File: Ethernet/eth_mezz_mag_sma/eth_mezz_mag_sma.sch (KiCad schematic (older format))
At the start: 13 parts, among them J1 Conn_01x09_Male, J2 TX-, J3 RX+, J4 RX-, J5 TX+

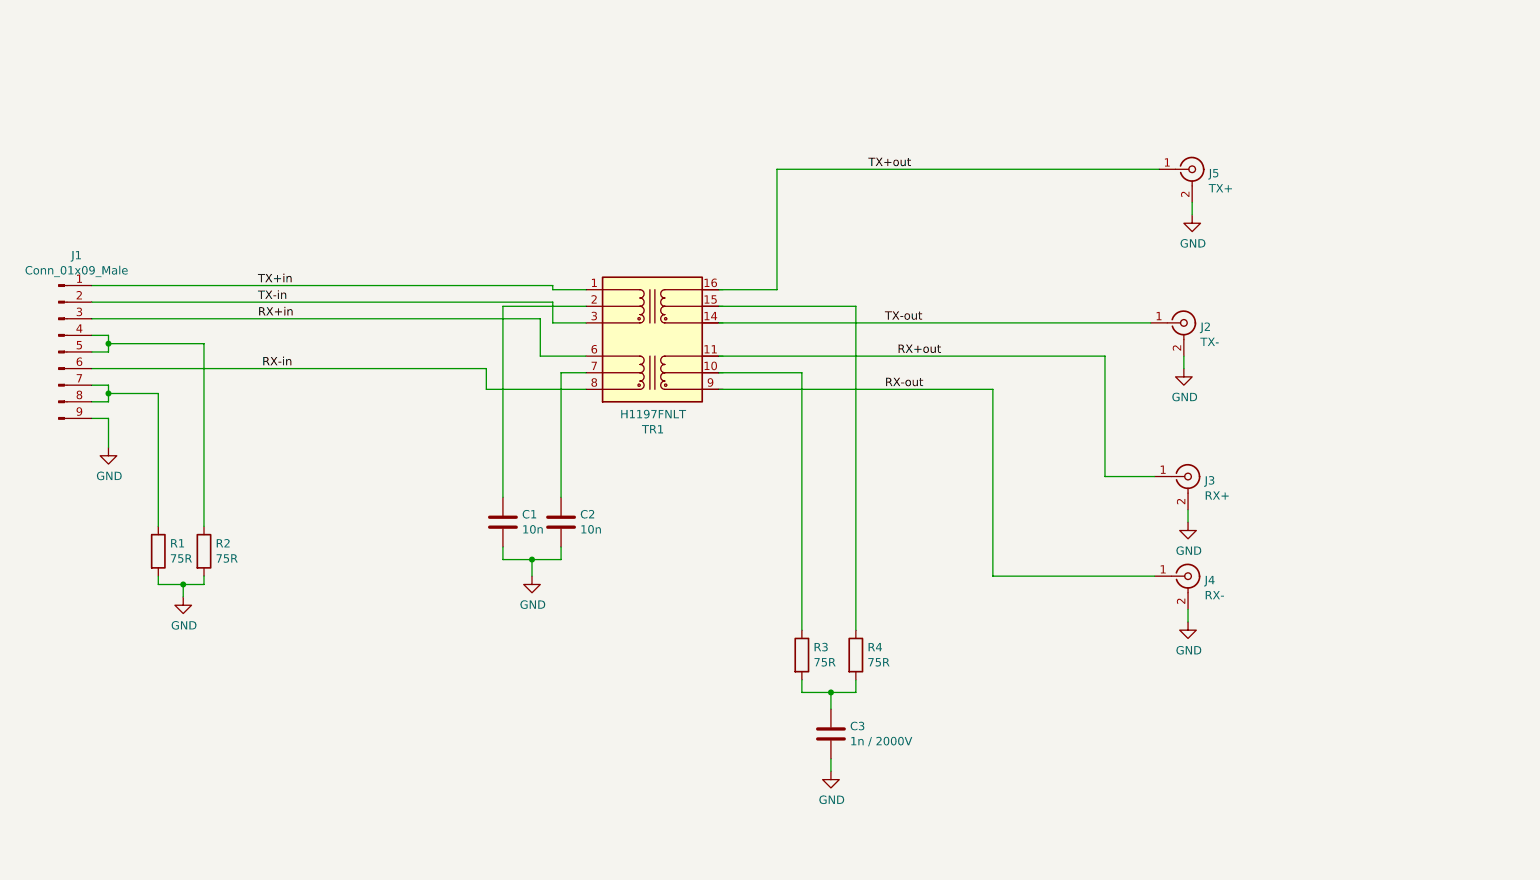
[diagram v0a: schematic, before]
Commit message: PHY module with RJ45
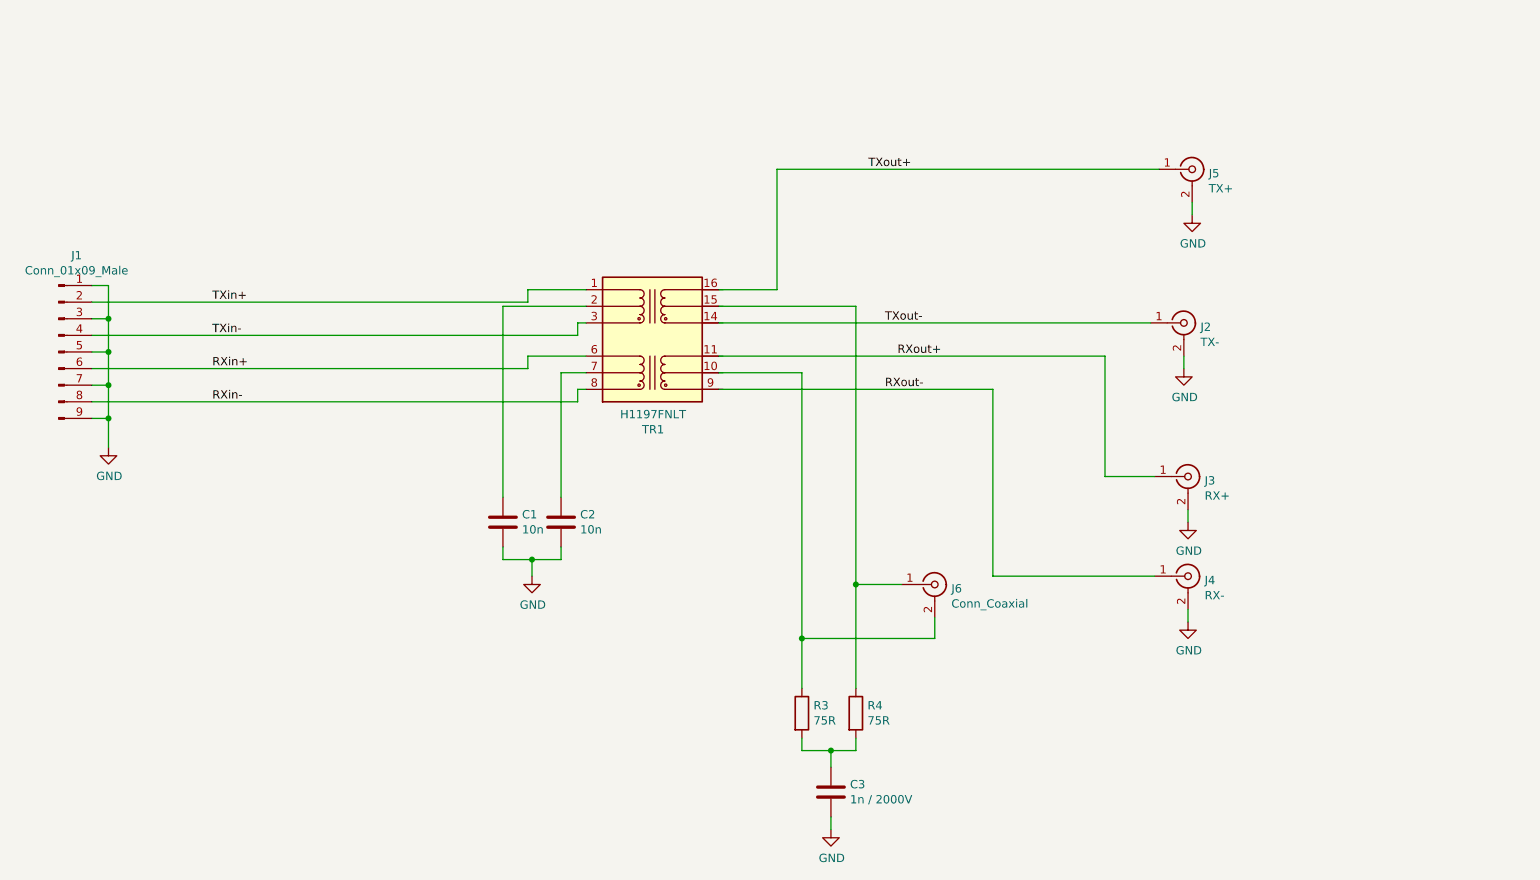
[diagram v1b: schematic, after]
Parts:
- removed R1, R2: 75R, Resistor_SMD:R_1206_3216Metric_Pad1.42x1.75mm_HandSolder, symbol Device:R
- added J6: Conn_Coaxial, Connector_Coaxial:BNC_TEConnectivity_1478204_Vertical, symbol Connector:Conn_Coaxial
- C1, C2: footprint Resistor_SMD:R_1206_3216Metric_Pad1.42x1.75mm_HandSolder -> Capacitor_SMD:C_0805_2012Metric_Pad1.18x1.45mm_HandSolder
- R3, R4: footprint Resistor_SMD:R_1206_3216Metric_Pad1.42x1.75mm_HandSolder -> Resistor_SMD:R_0805_2012Metric_Pad1.20x1.40mm_HandSolder
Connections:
- net GND: now also J1.1 (Pin_1), J1.3 (Pin_3), J1.5 (Pin_5), J1.7 (Pin_7)
- net at R3.1, TR1.10 (C_RX): now also J6.2 (Ext)
- net at R4.1, TR1.15 (C_TX): now also J6.1 (In)
- net TXin-: now reaches J1.4 (Pin_4)
- net TXin-: now also TR1.3 (TD-); no longer J1.5 (Pin_5)
- net RXin-: now reaches J1.8 (Pin_8)
- net RXin-: now also TR1.8 (RD-); no longer J1.7 (Pin_7)
- net RX+in renamed RXin+
- net RXin+: now also J1.6 (Pin_6); no longer J1.3 (Pin_3)
- net RX+out renamed RXout+
- removed net RX-in: J1.6 (Pin_6), TR1.8 (RD-)
- net RX-out renamed RXout-
- net TX+in renamed TXin+
- net TXin+: now also J1.2 (Pin_2); no longer J1.1 (Pin_1)
- net TX+out renamed TXout+
- removed net TX-in: J1.2 (Pin_2), TR1.3 (TD-)
- net TX-out renamed TXout-
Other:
- moved on the sheet: C3, R3, R4
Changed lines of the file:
@@
 L Device:R R3
 U 1 1 61BAD53E
-P 6275 4975
-F 0 "R3" H 6345 5021 50  0000 L CNN
-F 1 "75R" H 6345 4930 50  0000 L CNN
-F 2 "Resistor_SMD:R_1206_3216Metric_Pad1.42x1.75mm_HandSolder" V 6205 4975 50  0001 C CNN
-F 3 "~" H 6275 4975 50  0001 C CNN
-	1    6275 4975
+P 6275 5325
+F 0 "R3" H 6345 5371 50  0000 L CNN
+F 1 "75R" H 6345 5280 50  0000 L CNN
+F 2 "Resistor_SMD:R_0805_2012Metric_Pad1.20x1.40mm_HandSolder" V 6205 5325 50  0001 C CNN
+F 3 "~" H 6275 5325 50  0001 C CNN
+	1    6275 5325
 	1    0    0    -1
 $EndComp
@@
 L Device:R R4
 U 1 1 61BADB8B
-P 6600 4975
-F 0 "R4" H 6670 5021 50  0000 L CNN
-F 1 "75R" H 6670 4930 50  0000 L CNN
-F 2 "Resistor_SMD:R_1206_3216Metric_Pad1.42x1.75mm_HandSolder" V 6530 4975 50  0001 C CNN
-F 3 "~" H 6600 4975 50  0001 C CNN
-	1    6600 4975
+P 6600 5325
+F 0 "R4" H 6670 5371 50  0000 L CNN
+F 1 "75R" H 6670 5280 50  0000 L CNN
+F 2 "Resistor_SMD:R_0805_2012Metric_Pad1.20x1.40mm_HandSolder" V 6530 5325 50  0001 C CNN
+F 3 "~" H 6600 5325 50  0001 C CNN
+	1    6600 5325
 	1    0    0    -1
 $EndComp
@@
 L Device:C C3
 U 1 1 61BAE2C0
-P 6450 5450
-F 0 "C3" H 6565 5496 50  0000 L CNN
-F 1 "1n / 2000V" H 6565 5405 50  0000 L CNN
-F 2 "Resistor_SMD:R_1206_3216Metric_Pad1.42x1.75mm_HandSolder" H 6488 5300 50  0001 C CNN
-F 3 "~" H 6450 5450 50  0001 C CNN
-	1    6450 5450
+P 6450 5800
+F 0 "C3" H 6565 5846 50  0000 L CNN
+F 1 "1n / 2000V" H 6565 5755 50  0000 L CNN
+F 2 "Resistor_SMD:R_1206_3216Metric_Pad1.42x1.75mm_HandSolder" H 6488 5650 50  0001 C CNN
+F 3 "~" H 6450 5800 50  0001 C CNN
+	1    6450 5800
 	1    0    0    -1
 $EndComp
@@
 F 0 "C1" H 4590 4221 50  0000 L CNN
 F 1 "10n" H 4590 4130 50  0000 L CNN
-F 2 "Resistor_SMD:R_1206_3216Metric_Pad1.42x1.75mm_HandSolder" H 4513 4025 50  0001 C CNN
+F 2 "Capacitor_SMD:C_0805_2012Metric_Pad1.18x1.45mm_HandSolder" H 4513 4025 50  0001 C CNN
 F 3 "~" H 4475 4175 50  0001 C CNN
 	1    4475 4175
@@
 F 0 "C2" H 4940 4221 50  0000 L CNN
 F 1 "10n" H 4940 4130 50  0000 L CNN
-F 2 "Resistor_SMD:R_1206_3216Metric_Pad1.42x1.75mm_HandSolder" H 4863 4025 50  0001 C CNN
+F 2 "Capacitor_SMD:C_0805_2012Metric_Pad1.18x1.45mm_HandSolder" H 4863 4025 50  0001 C CNN
 F 3 "~" H 4825 4175 50  0001 C CNN
 	1    4825 4175
@@
 $EndComp
 Wire Wire Line
-	2000 2750 4775 2750
-Wire Wire Line
-	4775 2750 4775 2775
-Wire Wire Line
-	4775 2775 4975 2775
-Wire Wire Line
-	2000 2850 4775 2850
-Wire Wire Line
-	4775 2850 4775 2975
-Wire Wire Line
-	4775 2975 4975 2975
-Wire Wire Line
-	2000 2950 4700 2950
-Wire Wire Line
-	4700 2950 4700 3175
-Wire Wire Line
-	4700 3175 4975 3175
-Wire Wire Line
-	2000 3250 4375 3250
-Wire Wire Line
-	4375 3250 4375 3375
-Wire Wire Line
-	4375 3375 4975 3375
-Wire Wire Line
 	5775 2775 6125 2775
 Wire Wire Line
@@
 Wire Wire Line
 	7425 4500 8400 4500
-Wire Wire Line
-	4975 3275 4825 3275
-Wire Wire Line
-	4825 3275 4825 4025
-Wire Wire Line
-	4975 2875 4475 2875
-Wire Wire Line
-	4475 2875 4475 4025
-$Comp
-L Device:R R1
-U 1 1 61BB773B
-P 2400 4350
-F 0 "R1" H 2470 4396 50  0000 L CNN
-F 1 "75R" H 2470 4305 50  0000 L CNN
-F 2 "Resistor_SMD:R_1206_3216Metric_Pad1.42x1.75mm_HandSolder" V 2330 4350 50  0001 C CNN
-F 3 "~" H 2400 4350 50  0001 C CNN
-	1    2400 4350
-	1    0    0    -1
-$EndComp
-Wire Wire Line
-	2000 3050 2100 3050
-Wire Wire Line
-	2100 3050 2100 3100
-Wire Wire Line
-	2100 3150 2000 3150
-Wire Wire Line
-	2000 3350 2100 3350
-Wire Wire Line
-	2100 3350 2100 3400
-Wire Wire Line
-	2100 3450 2000 3450
 $Comp
 L power:GND #PWR01
@@
 Wire Wire Line
 	2000 3550 2100 3550
-Wire Wire Line
-	2100 3550 2100 3725
-Wire Wire Line
-	2400 4200 2400 3400
-Wire Wire Line
-	2400 3400 2100 3400
-Connection ~ 2100 3400
-Wire Wire Line
-	2100 3400 2100 3450
-$Comp
-L Device:R R2
-U 1 1 61BBA3B7
-P 2675 4350
-F 0 "R2" H 2745 4396 50  0000 L CNN
-F 1 "75R" H 2745 4305 50  0000 L CNN
-F 2 "Resistor_SMD:R_1206_3216Metric_Pad1.42x1.75mm_HandSolder" V 2605 4350 50  0001 C CNN
-F 3 "~" H 2675 4350 50  0001 C CNN
-	1    2675 4350
-	1    0    0    -1
-$EndComp
-Wire Wire Line
-	2675 4200 2675 3100
-Wire Wire Line
-	2675 3100 2100 3100
-Connection ~ 2100 3100
-Wire Wire Line
-	2100 3100 2100 3150
-$Comp
-L power:GND #PWR02
-U 1 1 61BBB0D3
-P 2550 4625
-F 0 "#PWR02" H 2550 4375 50  0001 C CNN
-F 1 "GND" H 2555 4452 50  0000 C CNN
-F 2 "" H 2550 4625 50  0001 C CNN
-F 3 "" H 2550 4625 50  0001 C CNN
-	1    2550 4625
-	1    0    0    -1
-$EndComp
-Wire Wire Line
-	2400 4500 2400 4550
-Wire Wire Line
-	2400 4550 2550 4550
-Wire Wire Line
-	2675 4550 2675 4500
-Connection ~ 2550 4550
-Wire Wire Line
-	2550 4550 2675 4550
-Wire Wire Line
-	2550 4550 2550 4625
 $Comp
 L power:GND #PWR03
@@
 	5775 2875 6600 2875
 Wire Wire Line
-	6600 2875 6600 4825
+	6600 2875 6600 4550
 Wire Wire Line
 	5775 3275 6275 3275
 Wire Wire Line
-	6275 3275 6275 4825
-Wire Wire Line
-	6275 5125 6275 5200
-Wire Wire Line
-	6275 5200 6450 5200
-Wire Wire Line
-	6600 5200 6600 5125
-Wire Wire Line
-	6450 5300 6450 5200
-Connection ~ 6450 5200
-Wire Wire Line
-	6450 5200 6600 5200
+	6275 3275 6275 4875
+Wire Wire Line
+	6275 5475 6275 5550
+Wire Wire Line
+	6275 5550 6450 5550
+Wire Wire Line
+	6600 5550 6600 5475
+Wire Wire Line
+	6450 5650 6450 5550
+Connection ~ 6450 5550
+Wire Wire Line
+	6450 5550 6600 5550
 $Comp
 L power:GND #PWR04
 U 1 1 61BC3E53
-P 6450 5675
-F 0 "#PWR04" H 6450 5425 50  0001 C CNN
-F 1 "GND" H 6455 5502 50  0000 C CNN
-F 2 "" H 6450 5675 50  0001 C CNN
-F 3 "" H 6450 5675 50  0001 C CNN
-	1    6450 5675
-	1    0    0    -1
-$EndComp
-Wire Wire Line
-	6450 5600 6450 5675
+P 6450 6025
+F 0 "#PWR04" H 6450 5775 50  0001 C CNN
+F 1 "GND" H 6455 5852 50  0000 C CNN
+F 2 "" H 6450 6025 50  0001 C CNN
+F 3 "" H 6450 6025 50  0001 C CNN
+	1    6450 6025
+	1    0    0    -1
+$EndComp
+Wire Wire Line
+	6450 5950 6450 6025
 $Comp
 L power:GND #PWR07
@@
 Wire Wire Line
 	8600 4700 8600 4775
-Text Label 3000 2750 0    50   ~ 0
-TX+in
-Text Label 3000 2850 0    50   ~ 0
-TX-in
-Text Label 3000 2950 0    50   ~ 0
-RX+in
-Text Label 3025 3250 0    50   ~ 0
-RX-in
+Text Label 2725 2850 0    50   ~ 0
+TXin+
+Text Label 2725 3050 0    50   ~ 0
+TXin-
+Text Label 2725 3250 0    50   ~ 0
+RXin+
+Text Label 2725 3450 0    50   ~ 0
+RXin-
 Text Label 6675 2050 0    50   ~ 0
-TX+out
+TXout+
 Text Label 6775 2975 0    50   ~ 0
-TX-out
+TXout-
 Text Label 6850 3175 0    50   ~ 0
-RX+out
+RXout+
 Text Label 6775 3375 0    50   ~ 0
-RX-out
+RXout-
+Wire Wire Line
+	2000 2850 4625 2850
+Wire Wire Line
+	4625 2850 4625 2775
+Wire Wire Line
+	4625 2775 4975 2775
+Wire Wire Line
+	2000 3050 4925 3050
+Wire Wire Line
+	4925 3050 4925 2975
+Wire Wire Line
+	4925 2975 4975 2975
+Wire Wire Line
+	2000 3250 4625 3250
+Wire Wire Line
+	4625 3250 4625 3175
+Wire Wire Line
+	4625 3175 4975 3175
+Wire Wire Line
+	2000 3450 4925 3450
+Wire Wire Line
+	4925 3450 4925 3375
+Wire Wire Line
+	4925 3375 4975 3375
+Wire Wire Line
+	4975 3275 4825 3275
+Wire Wire Line
+	4825 3275 4825 4025
+Wire Wire Line
+	4975 2875 4475 2875
+Wire Wire Line
+	4475 2875 4475 4025
+Wire Wire Line
+	2000 2750 2100 2750
+Wire Wire Line
+	2100 2750 2100 2950
+Connection ~ 2100 3550
+Wire Wire Line
+	2100 3550 2100 3725
+Wire Wire Line
+	2000 2950 2100 2950
+Connection ~ 2100 2950
+Wire Wire Line
+	2100 2950 2100 3150
+Wire Wire Line
+	2000 3150 2100 3150
+Connection ~ 2100 3150
+Wire Wire Line
+	2100 3150 2100 3350
+Wire Wire Line
+	2000 3350 2100 3350
+Connection ~ 2100 3350
+Wire Wire Line
+	2100 3350 2100 3550
+$Comp
+L Connector:Conn_Coaxial J6
+U 1 1 61BA50FC
+P 7075 4550
+F 0 "J6" H 7175 4525 50  0000 L CNN
+F 1 "Conn_Coaxial" H 7175 4434 50  0000 L CNN
+F 2 "Connector_Coaxial:BNC_TEConnectivity_1478204_Vertical" H 7075 4550 50  0001 C CNN
+F 3 " ~" H 7075 4550 50  0001 C CNN
+	1    7075 4550
+	1    0    0    -1
+$EndComp
+Wire Wire Line
+	6875 4550 6600 4550
+Connection ~ 6600 4550
+Wire Wire Line
+	6600 4550 6600 5175
+Wire Wire Line
+	7075 4750 7075 4875
+Wire Wire Line
+	7075 4875 6275 4875
+Connection ~ 6275 4875
+Wire Wire Line
+	6275 4875 6275 5175
 $EndSCHEMATC

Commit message: SomeBoardsReady
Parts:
- added H1, H2: MountingHole_Pad, MountingHole:MountingHole_3.2mm_M3_Pad_Via, symbol Mechanical:MountingHole_Pad
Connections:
- net labels added: RCT, TCT
- wire segments 60 -> 66
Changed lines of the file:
@@
 L power:GND #PWR01
 U 1 1 61BB909F
-P 2100 3725
-F 0 "#PWR01" H 2100 3475 50  0001 C CNN
-F 1 "GND" H 2105 3552 50  0000 C CNN
-F 2 "" H 2100 3725 50  0001 C CNN
-F 3 "" H 2100 3725 50  0001 C CNN
-	1    2100 3725
-	1    0    0    -1
-$EndComp
-Wire Wire Line
-	2000 3550 2100 3550
+P 2250 4000
+F 0 "#PWR01" H 2250 3750 50  0001 C CNN
+F 1 "GND" H 2255 3827 50  0000 C CNN
+F 2 "" H 2250 4000 50  0001 C CNN
+F 3 "" H 2250 4000 50  0001 C CNN
+	1    2250 4000
+	1    0    0    -1
+$EndComp
 $Comp
 L power:GND #PWR03
@@
 RXout-
 Wire Wire Line
-	2000 2850 4625 2850
-Wire Wire Line
-	4625 2850 4625 2775
-Wire Wire Line
-	4625 2775 4975 2775
-Wire Wire Line
-	2000 3050 4925 3050
-Wire Wire Line
-	4925 3050 4925 2975
-Wire Wire Line
-	4925 2975 4975 2975
-Wire Wire Line
-	2000 3250 4625 3250
-Wire Wire Line
-	4625 3250 4625 3175
-Wire Wire Line
-	4625 3175 4975 3175
-Wire Wire Line
-	2000 3450 4925 3450
-Wire Wire Line
-	4925 3450 4925 3375
-Wire Wire Line
-	4925 3375 4975 3375
+	2000 2850 4075 2850
+Wire Wire Line
+	4075 2850 4075 2775
+Wire Wire Line
+	4075 2775 4975 2775
+Wire Wire Line
+	2000 3050 4075 3050
+Wire Wire Line
+	4075 3050 4075 2975
+Wire Wire Line
+	4075 2975 4975 2975
+Wire Wire Line
+	2000 3250 4075 3250
+Wire Wire Line
+	4075 3250 4075 3175
+Wire Wire Line
+	4075 3175 4975 3175
+Wire Wire Line
+	2000 3450 4075 3450
+Wire Wire Line
+	4075 3450 4075 3375
+Wire Wire Line
+	4075 3375 4975 3375
 Wire Wire Line
 	4975 3275 4825 3275
@@
 	4475 2875 4475 4025
 Wire Wire Line
-	2000 2750 2100 2750
-Wire Wire Line
-	2100 2750 2100 2950
-Connection ~ 2100 3550
-Wire Wire Line
-	2100 3550 2100 3725
-Wire Wire Line
-	2000 2950 2100 2950
-Connection ~ 2100 2950
-Wire Wire Line
-	2100 2950 2100 3150
-Wire Wire Line
-	2000 3150 2100 3150
-Connection ~ 2100 3150
-Wire Wire Line
-	2100 3150 2100 3350
-Wire Wire Line
-	2000 3350 2100 3350
-Connection ~ 2100 3350
-Wire Wire Line
-	2100 3350 2100 3550
+	2000 2750 2175 2750
+Wire Wire Line
+	2000 2950 2250 2950
+Wire Wire Line
+	2250 2950 2250 3150
+Wire Wire Line
+	2000 3150 2250 3150
+Connection ~ 2250 3150
+Wire Wire Line
+	2250 3150 2250 3350
+Wire Wire Line
+	2000 3350 2250 3350
+Connection ~ 2250 3350
 $Comp
 L Connector:Conn_Coaxial J6
@@
 Wire Wire Line
 	6275 4875 6275 5175
+Text Label 4475 2875 0    50   ~ 0
+TCT
+Text Label 4825 3275 0    50   ~ 0
+RCT
+Text Label 2175 2750 2    50   ~ 0
+TCT
+Wire Wire Line
+	2250 3350 2250 3825
+Wire Wire Line
+	2000 3550 2200 3550
+Text Label 2200 3550 2    50   ~ 0
+RCT
+$Comp
+L power:PWR_FLAG #FLG0101
+U 1 1 61BC2B9D
+P 2575 3700
+F 0 "#FLG0101" H 2575 3775 50  0001 C CNN
+F 1 "PWR_FLAG" H 2575 3873 50  0000 C CNN
+F 2 "" H 2575 3700 50  0001 C CNN
+F 3 "~" H 2575 3700 50  0001 C CNN
+	1    2575 3700
+	1    0    0    -1
+$EndComp
+Wire Wire Line
+	2575 3700 2575 3825
+Wire Wire Line
+	2575 3825 2250 3825
+Connection ~ 2250 3825
+Wire Wire Line
+	2250 3825 2250 4000
+$Comp
+L Mechanical:MountingHole_Pad H2
+U 1 1 61BCB346
+P 10050 1700
+F 0 "H2" H 10150 1749 50  0000 L CNN
+F 1 "MountingHole_Pad" H 10150 1658 50  0000 L CNN
+F 2 "MountingHole:MountingHole_3.2mm_M3_Pad_Via" H 10050 1700 50  0001 C CNN
+F 3 "~" H 10050 1700 50  0001 C CNN
+	1    10050 1700
+	1    0    0    -1
+$EndComp
+$Comp
+L Mechanical:MountingHole_Pad H1
+U 1 1 61BCB6A3
+P 9200 1700
+F 0 "H1" H 9300 1749 50  0000 L CNN
+F 1 "MountingHole_Pad" H 9300 1658 50  0000 L CNN
+F 2 "MountingHole:MountingHole_3.2mm_M3_Pad_Via" H 9200 1700 50  0001 C CNN
+F 3 "~" H 9200 1700 50  0001 C CNN
+	1    9200 1700
+	1    0    0    -1
+$EndComp
+$Comp
+L power:GND #PWR02
+U 1 1 61BCBDE5
+P 9600 2100
+F 0 "#PWR02" H 9600 1850 50  0001 C CNN
+F 1 "GND" H 9605 1927 50  0000 C CNN
+F 2 "" H 9600 2100 50  0001 C CNN
+F 3 "" H 9600 2100 50  0001 C CNN
+	1    9600 2100
+	1    0    0    -1
+$EndComp
+Wire Wire Line
+	9200 1800 9200 1925
+Wire Wire Line
+	9200 1925 9600 1925
+Wire Wire Line
+	10050 1925 10050 1800
+Wire Wire Line
+	9600 2100 9600 1925
+Connection ~ 9600 1925
+Wire Wire Line
+	9600 1925 10050 1925
 $EndSCHEMATC
